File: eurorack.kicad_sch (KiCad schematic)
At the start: 19 parts, among them J1 Eurorack 10-pin power, J2 to carrier row A (female 8.5m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, J3 to carrier row B (female 8.5m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, J4 to hat, above J2 (male), J5 to hat, above J3 (male), J6 IN 3.5mm mono, J7 OUT 3.5mm mono, J8 wires to hat J1/J2 pads, U1 K7805-1000R3

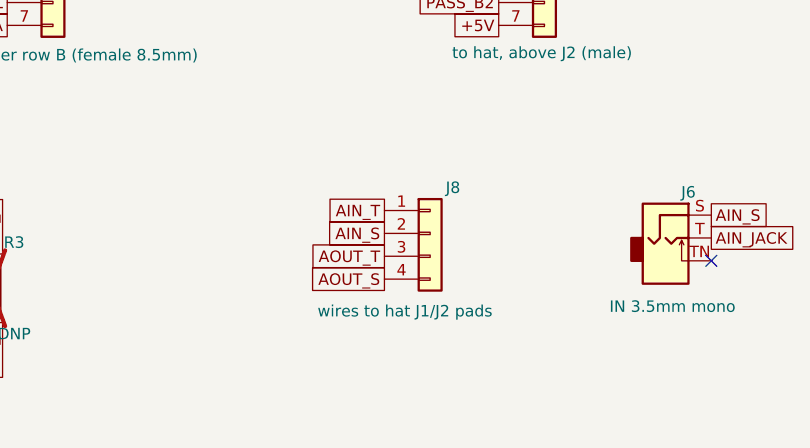
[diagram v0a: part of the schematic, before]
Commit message: J8 direct-mates hat J7: ground-between-signals pin order (swap 3/4), docs
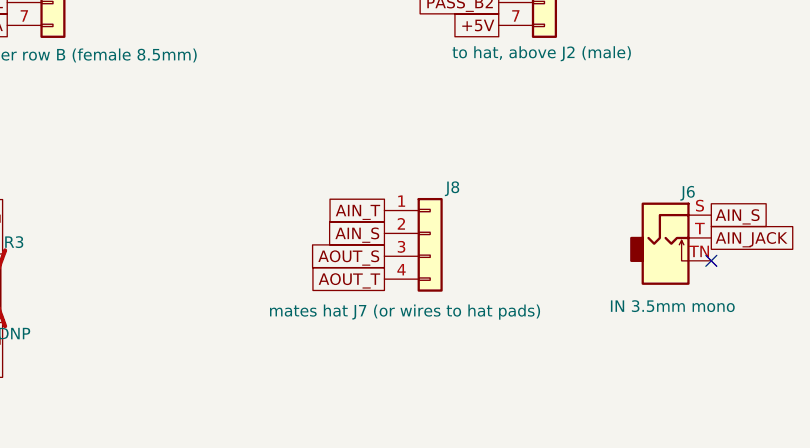
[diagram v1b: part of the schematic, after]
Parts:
- J8: value wires to hat J1/J2 pads -> mates hat J7 (or wires to hat pads)
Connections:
- net AOUT_S: now also J8.3 (Pin_3); no longer J8.4 (Pin_4)
- net AOUT_T: now also J8.4 (Pin_4); no longer J8.3 (Pin_3)

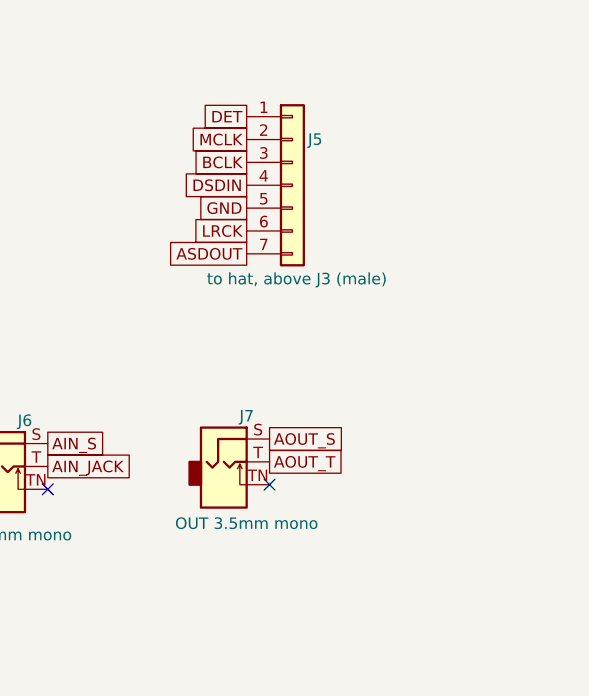
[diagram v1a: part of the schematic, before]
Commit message: display pass-through: J9 mates hat J6, J10 display socket, isolated DISP_* nets
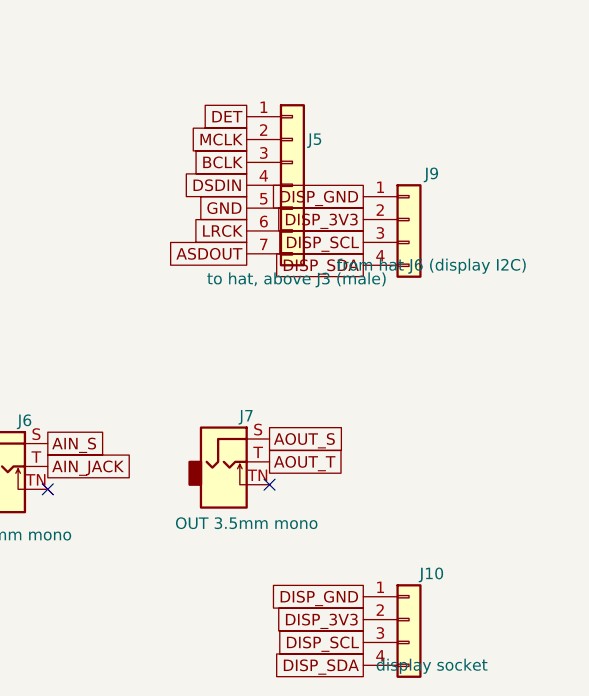
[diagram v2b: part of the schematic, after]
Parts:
- added J10: display socket, Connector_PinSocket_2.54mm:PinSocket_1x04_P2.54mm_Vertical, symbol Connector_Generic:Conn_01x04
- added J9: from hat J6 (display I2C), Connector_PinSocket_2.54mm:PinSocket_1x04_P2.54mm_Vertical, symbol Connector_Generic:Conn_01x04
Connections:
- new net DISP_3V3: J10.2 (Pin_2), J9.2 (Pin_2)
- new net DISP_GND: J10.1 (Pin_1), J9.1 (Pin_1)
- new net DISP_SCL: J10.3 (Pin_3), J9.3 (Pin_3)
- new net DISP_SDA: J10.4 (Pin_4), J9.4 (Pin_4)

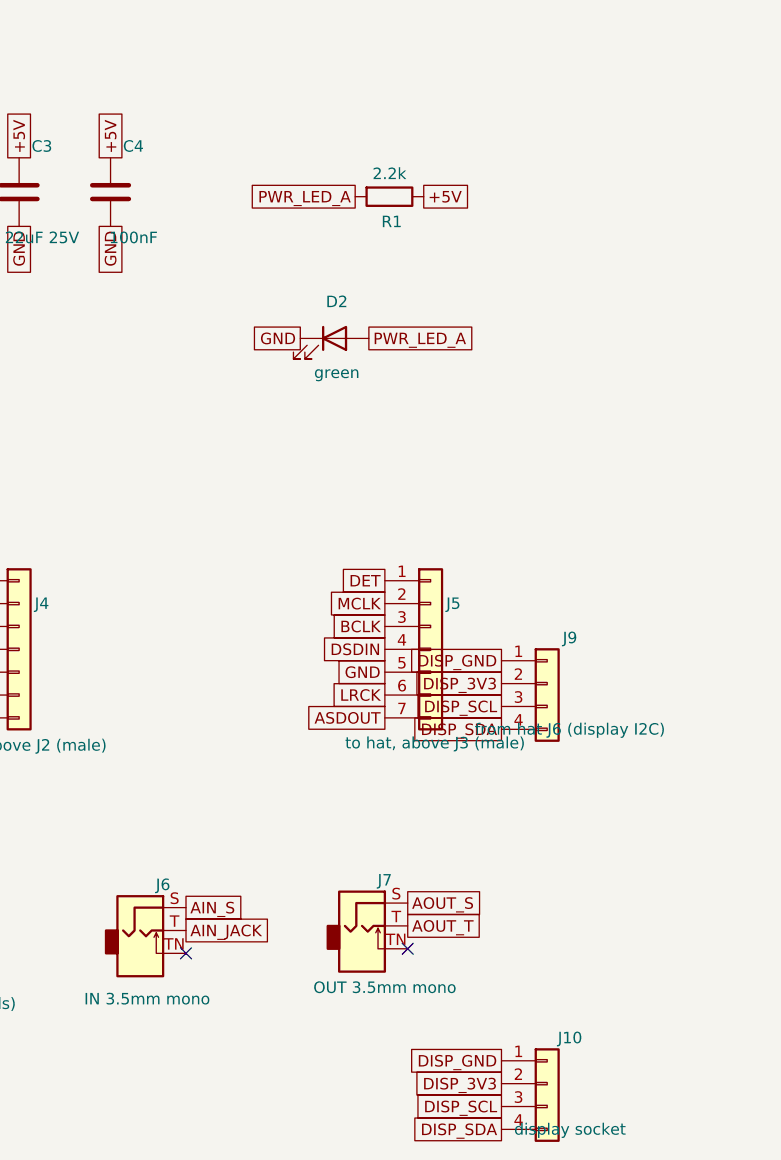
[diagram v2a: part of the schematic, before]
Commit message: layout: place and route the board; drop power LED and J9; display on main nets
- all nets routed, DRC clean (0 unconnected); audio in/out routed as tight
  signal+return pairs, input and output paths >=7mm apart
- single B.Cu GND pour over power + crossover; audio island pour-free,
  AIN_S/AOUT_S kept as separate returns end to end
- DISP_* nets merged into GND/+3V3/SCL/SDA: J10 powers and drives the
  display directly, hat J6 unneeded; J9 pass-through removed as redundant
- D2/R1 power LED dropped during layout; BOM synced
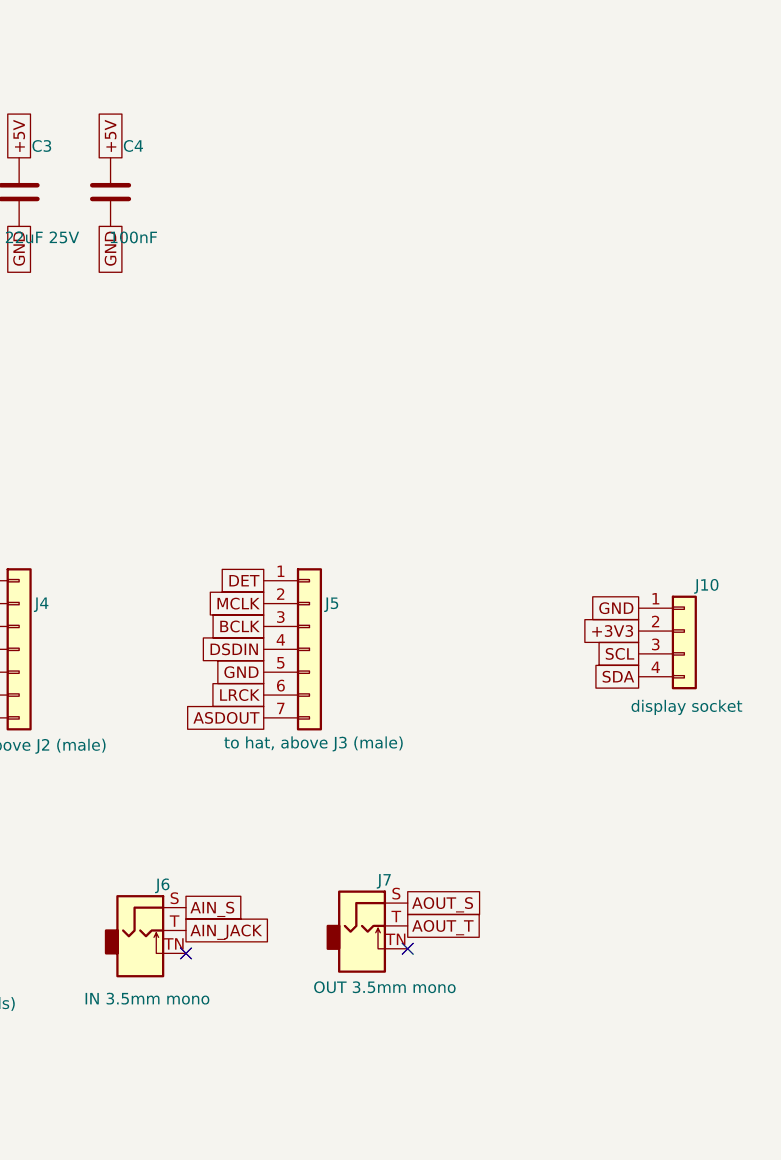
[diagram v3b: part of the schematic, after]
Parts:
- removed D2: green, LED_SMD:LED_0805_2012Metric, symbol Device:LED
- removed J9: from hat J6 (display I2C), Connector_PinSocket_2.54mm:PinSocket_1x04_P2.54mm_Vertical, symbol Connector_Generic:Conn_01x04
- removed R1: 2.2k, Resistor_SMD:R_0402_1005Metric, symbol Device:R
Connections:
- net DISP_3V3 is gone; now on net +3V3: J10.2 (Pin_2)
- net DISP_GND is gone; now on net GND: J10.1 (Pin_1)
- net DISP_SCL is gone; now on net SCL: J10.3 (Pin_3)
- net DISP_SDA is gone; now on net SDA: J10.4 (Pin_4)
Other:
- moved on the sheet: J10, J5

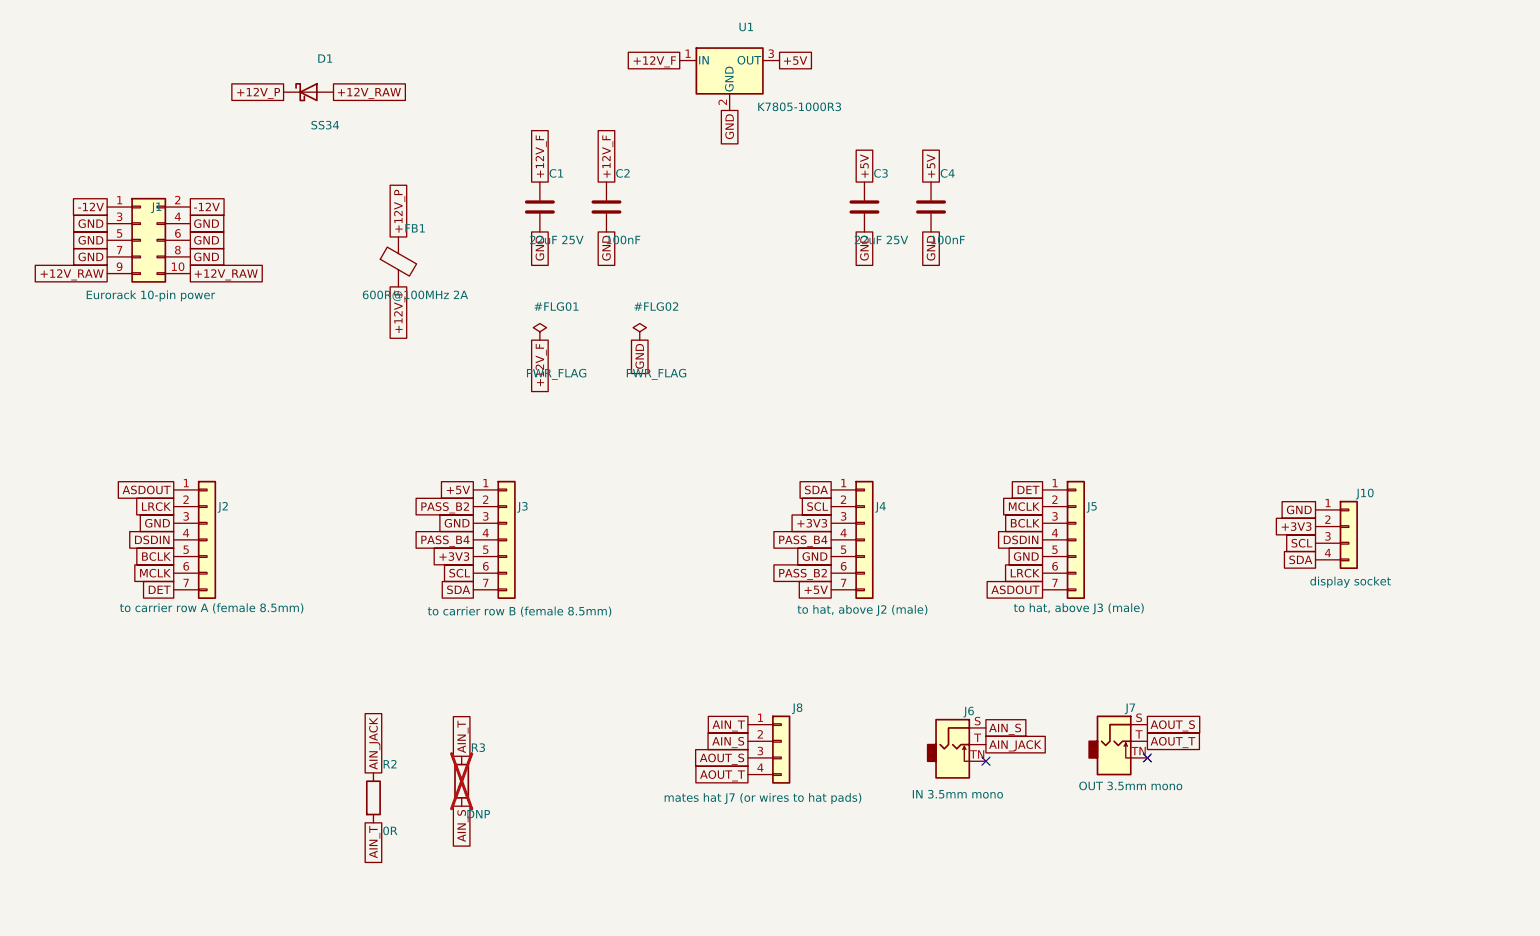
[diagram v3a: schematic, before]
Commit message: sch+pcb: eurorack I/O stage — input pad 100k/39k, TL072 x4.9 output amp on ±12V
- input divider now populated (R2/R3 = 100k/39k, -11.5dB): ±5V modular
  swings land inside the hat codec range; also protects against CV/gate
  mis-patches. Guitar-level alternative (R2=0R, R3 off) documented
- output: TL072 (C6961) x4.9 on +12V_F and a newly conditioned -12V rail
  (D2 SS34 + FB2 bead + 100n/22u), hat ~2Vpp -> ~10Vpp modular level,
  1k series out; spare half terminated; AOUT_S bonded to GND at one
  point (NT1 net tie); PWR_FLAG on -12V_F
- all new parts placed + routed, DRC clean; audit: no aggressors near
  the input pair, amp output >=3mm from input path everywhere
- fp-lib-table: add Package_SO + NetTie; BOM: 3 new lines (all LCSC
  in-stock verified), R2/R7 and R3/R5 share parts; ~45c/board added
- fab regen (CPL 19 placements, no DNP); verify D1/D2/U2 rotations in
  JLC preview; doc PDFs + STEP regenerated
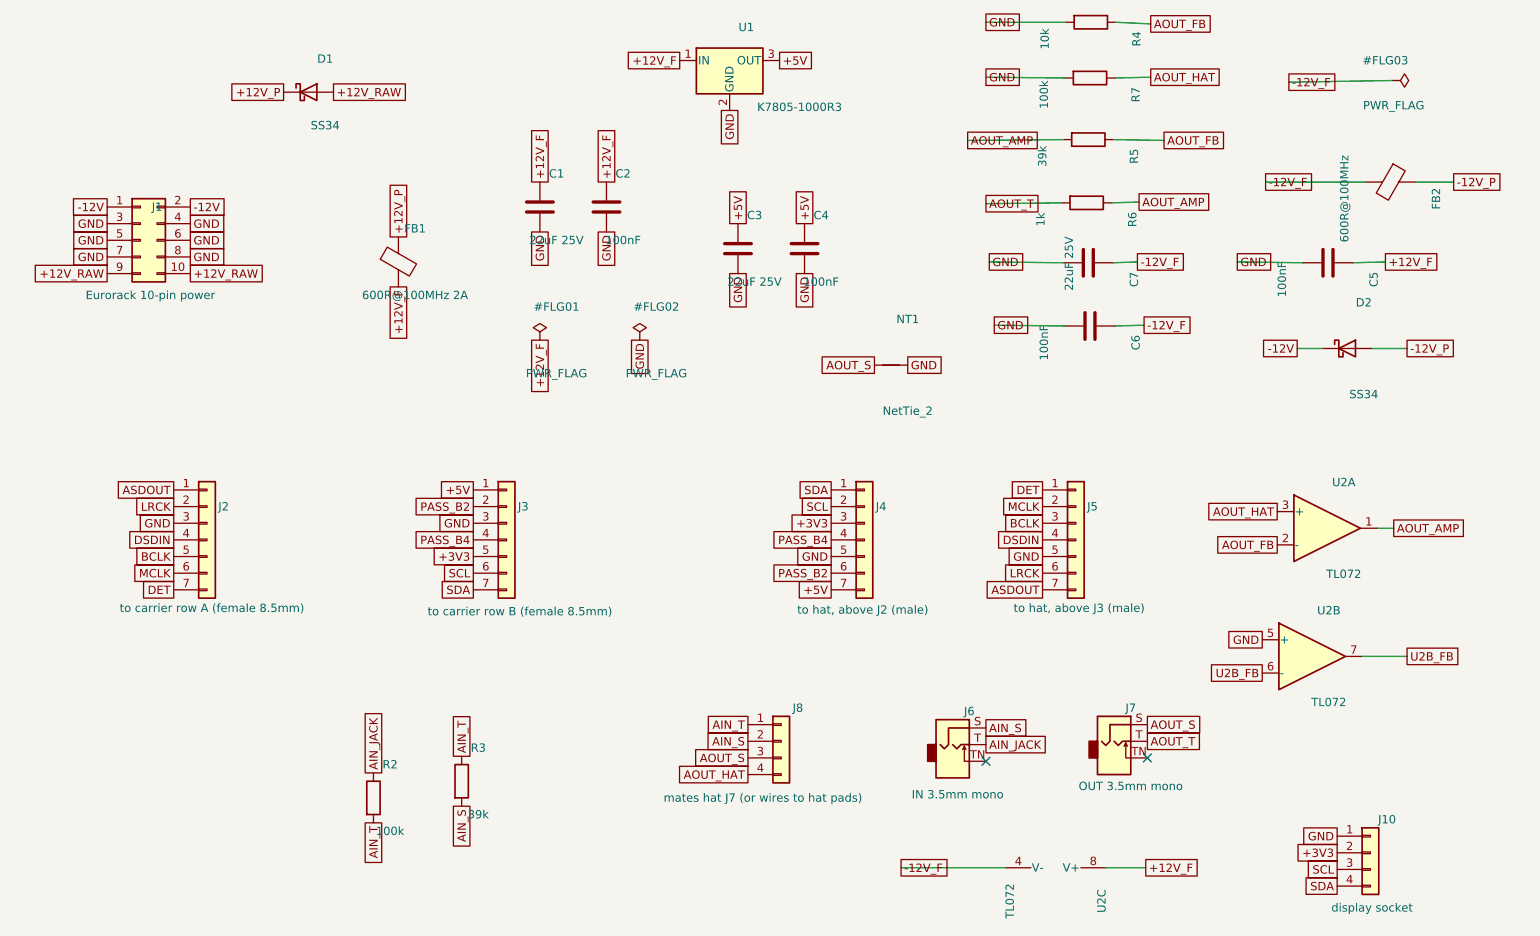
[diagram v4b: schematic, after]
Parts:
- added C5, C6: 100nF, Capacitor_SMD:C_0402_1005Metric, symbol Device:C
- added C7: 22uF 25V, Capacitor_SMD:C_0805_2012Metric, symbol Device:C
- added D2: SS34, Diode_SMD:D_SMA, symbol Device:D_Schottky
- added FB2: 600R@100MHz, Inductor_SMD:L_0805_2012Metric, symbol Device:FerriteBead
- added NT1: NetTie_2, NetTie:NetTie-2_SMD_Pad0.5mm, symbol Device:NetTie_2
- added R4: 10k, Resistor_SMD:R_0402_1005Metric, symbol Device:R
- added R5: 39k, Resistor_SMD:R_0402_1005Metric, symbol Device:R
- added R6: 1k, Resistor_SMD:R_0402_1005Metric, symbol Device:R
- added R7: 100k, Resistor_SMD:R_0402_1005Metric, symbol Device:R
- added U2: TL072, Package_SO:SOIC-8_3.9x4.9mm_P1.27mm, symbol Amplifier_Operational:TL072
- R2: value 0R -> 100k
- R3: value DNP -> 39k; now fitted
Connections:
- net +12V_F: now also C5.1, U2.8 (V+)
- net -12V: now also D2.1 (K)
- net AOUT_S: now also NT1.1
- net AOUT_T: now also R6.2; no longer J8.4 (Pin_4)
- net GND: now also C5.2, C6.2, C7.2, NT1.2, R4.2, R7.2, U2.5 (+)
- new net -12V_F: C6.1, C7.1, FB2.2, U2.4 (V-)
- new net -12V_P: D2.2 (A), FB2.1
- new net AOUT_AMP: R5.2, R6.1, U2.1
- new net AOUT_FB: R4.1, R5.1, U2.2 (-)
- new net AOUT_HAT: J8.4 (Pin_4), R7.1, U2.3 (+)
- new net U2B_FB: U2.6 (-), U2.7
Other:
- moved on the sheet: C3, C4, J10

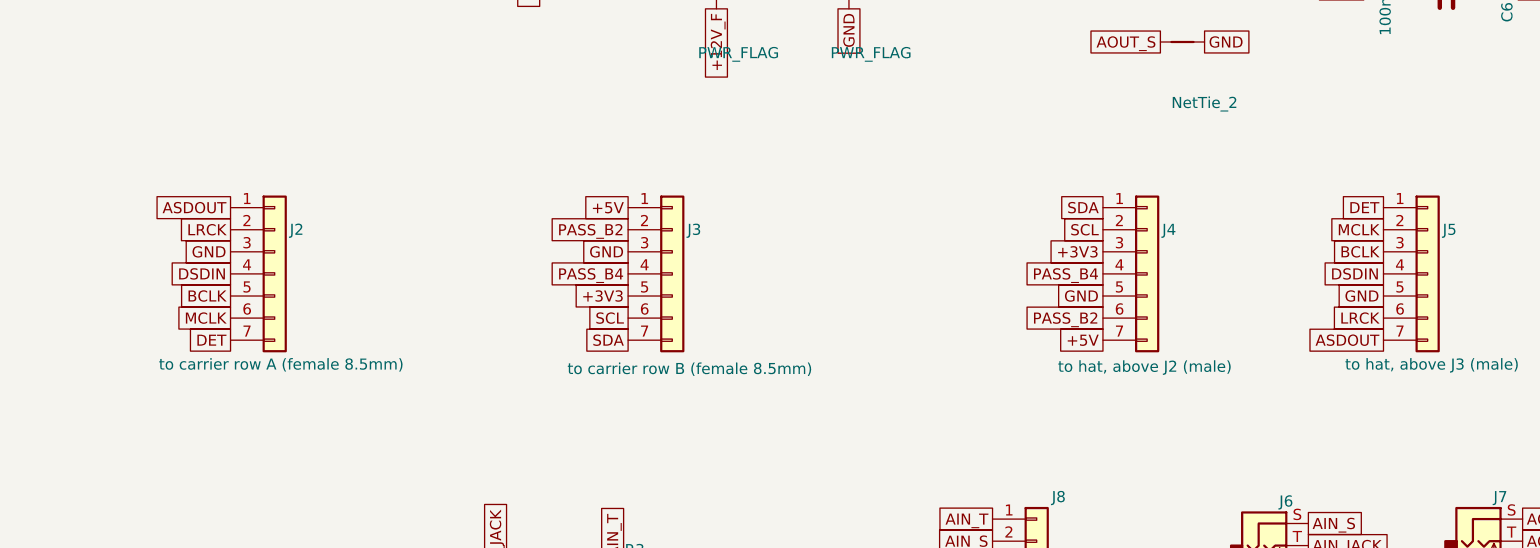
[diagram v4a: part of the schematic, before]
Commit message: sch+pcb: follow hat dual-host pinout — crossover net renames, J10 display taps moved to row-A I2C runs; regen fab + docs; add pinout graphic
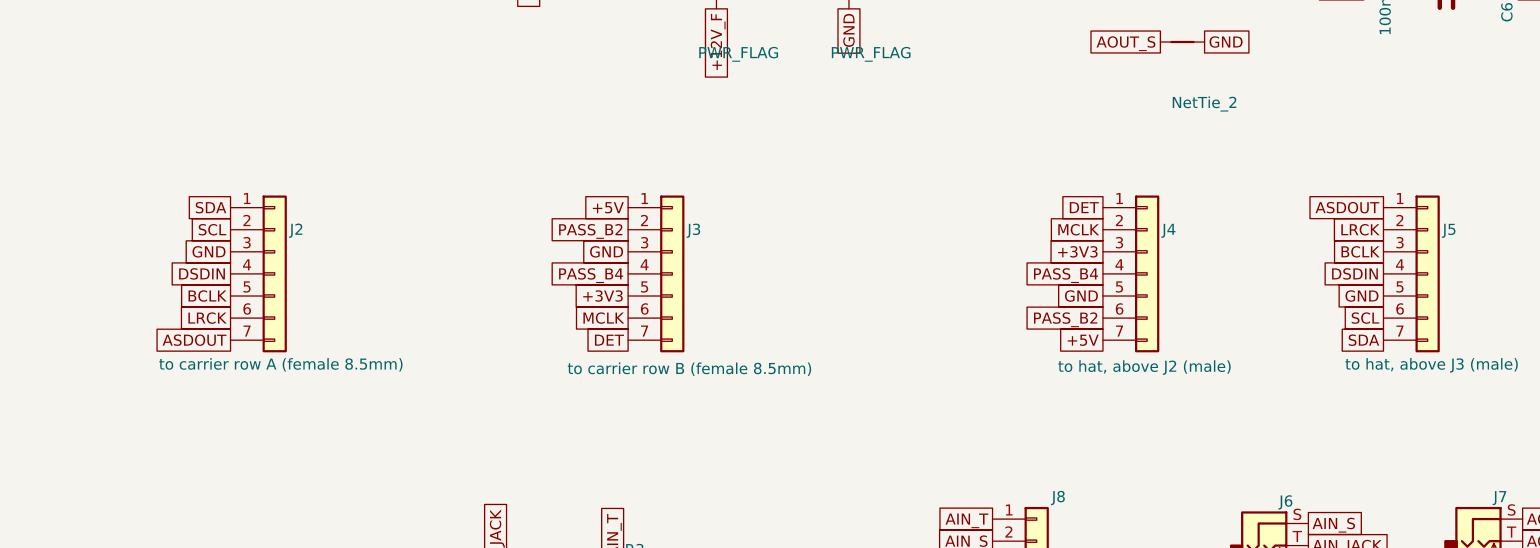
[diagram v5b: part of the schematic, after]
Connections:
- net ASDOUT: now also J2.7 (Pin_7), J5.1 (Pin_1); no longer J2.1 (Pin_1), J5.7 (Pin_7)
- net DET: now also J3.7 (Pin_7), J4.1 (Pin_1); no longer J2.7 (Pin_7), J5.1 (Pin_1)
- net LRCK: now also J2.6 (Pin_6), J5.2 (Pin_2); no longer J2.2 (Pin_2), J5.6 (Pin_6)
- net MCLK: now also J3.6 (Pin_6), J4.2 (Pin_2); no longer J2.6 (Pin_6), J5.2 (Pin_2)
- net SCL: now also J2.2 (Pin_2), J5.6 (Pin_6); no longer J3.6 (Pin_6), J4.2 (Pin_2)
- net SDA: now also J2.1 (Pin_1), J5.7 (Pin_7); no longer J3.7 (Pin_7), J4.1 (Pin_1)
